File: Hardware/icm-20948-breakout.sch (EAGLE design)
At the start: 11 parts, among them J1 455-1750-1-ND, J2 455-1750-1-ND, U1 NCP563, U2 NTS0104, U3 ICM-20948

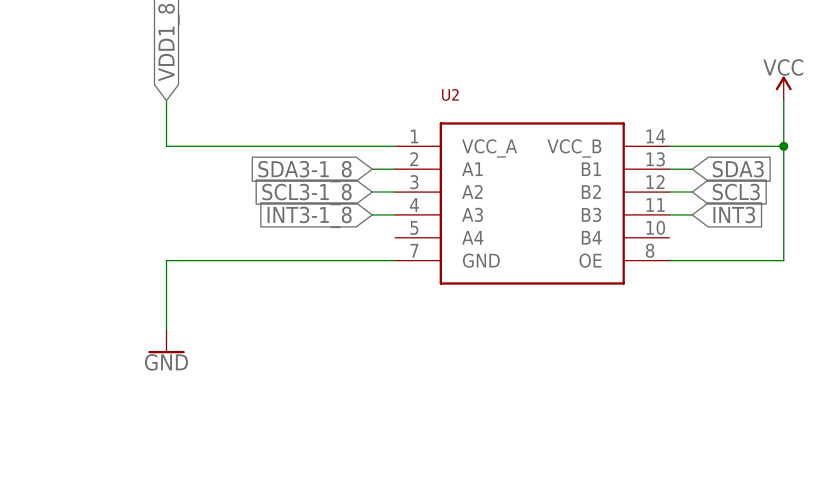
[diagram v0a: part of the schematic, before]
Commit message: Connected unused io pins on the level translator to ground.
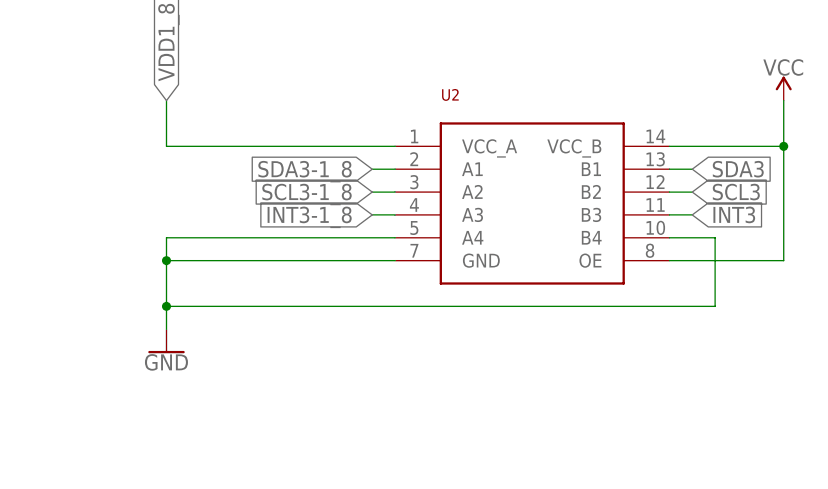
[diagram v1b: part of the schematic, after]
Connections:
- net GND: now also U2.A4, U2.B4
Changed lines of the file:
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@@
 <pinref part="GND4" gate="1" pin="GND"/>
 <pinref part="U2" gate="G$1" pin="GND"/>
-<wire x1="66.04" y1="20.32" x2="66.04" y2="12.7" width="0.1524" layer="91"/>
+<wire x1="66.04" y1="20.32" x2="66.04" y2="15.24" width="0.1524" layer="91"/>
+<wire x1="66.04" y1="15.24" x2="66.04" y2="12.7" width="0.1524" layer="91"/>
 <wire x1="91.44" y1="20.32" x2="66.04" y2="20.32" width="0.1524" layer="91"/>
+<pinref part="U2" gate="G$1" pin="A4"/>
+<wire x1="91.44" y1="22.86" x2="66.04" y2="22.86" width="0.1524" layer="91"/>
+<wire x1="66.04" y1="22.86" x2="66.04" y2="20.32" width="0.1524" layer="91"/>
+<junction x="66.04" y="20.32"/>
+<pinref part="U2" gate="G$1" pin="B4"/>
+<wire x1="121.92" y1="22.86" x2="127" y2="22.86" width="0.1524" layer="91"/>
+<wire x1="127" y1="22.86" x2="127" y2="15.24" width="0.1524" layer="91"/>
+<wire x1="127" y1="15.24" x2="66.04" y2="15.24" width="0.1524" layer="91"/>
+<junction x="66.04" y="15.24"/>
 </segment>
 <segment>

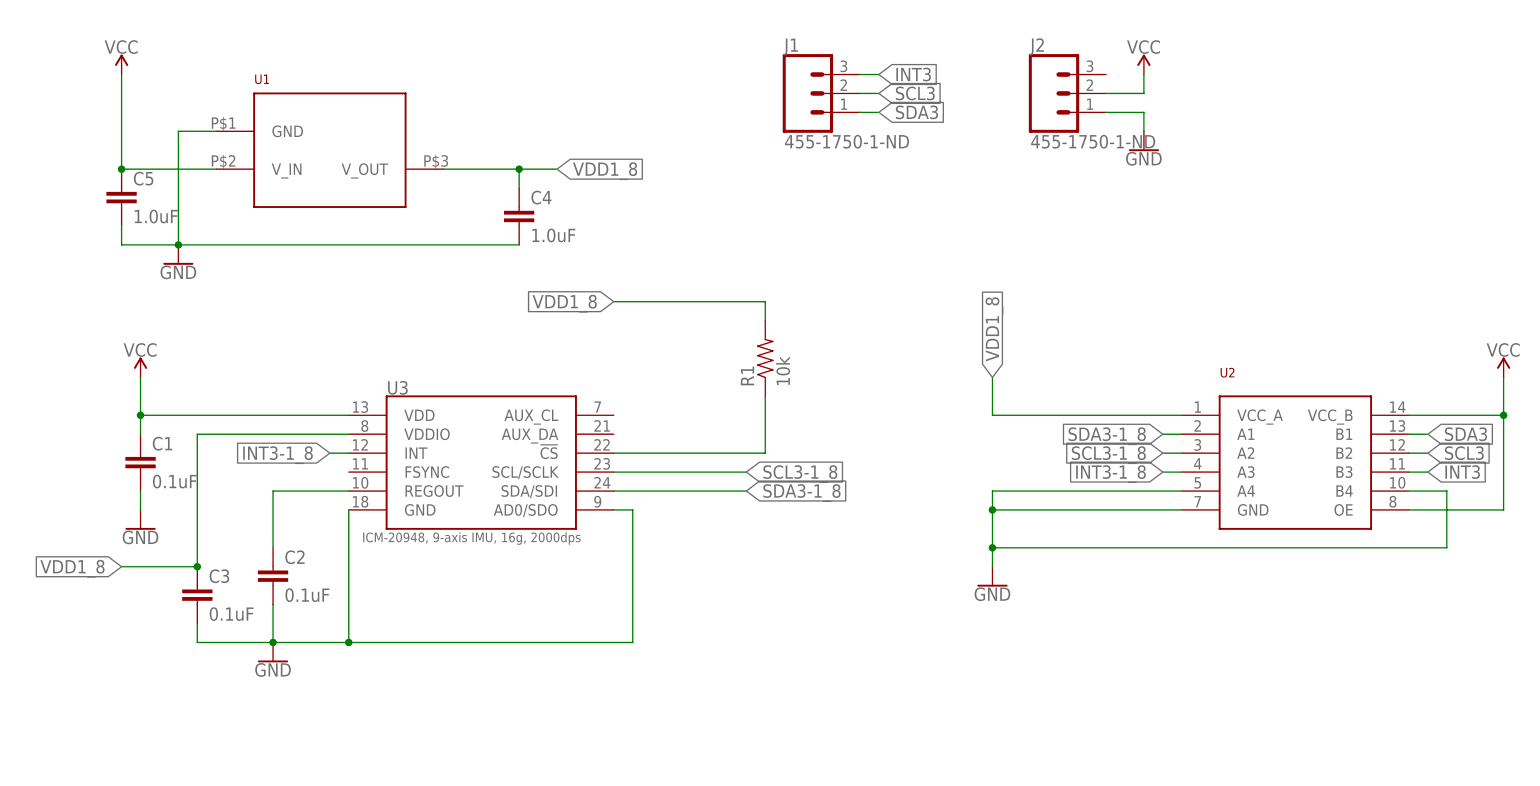
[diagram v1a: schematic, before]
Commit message: Redesign after comments. Changed footprints of capacitors. Removed routing under ICS. Connected nCS to level switcher to avoid a resistor. Added solder jumper to set address. Added ground planes on both sides.
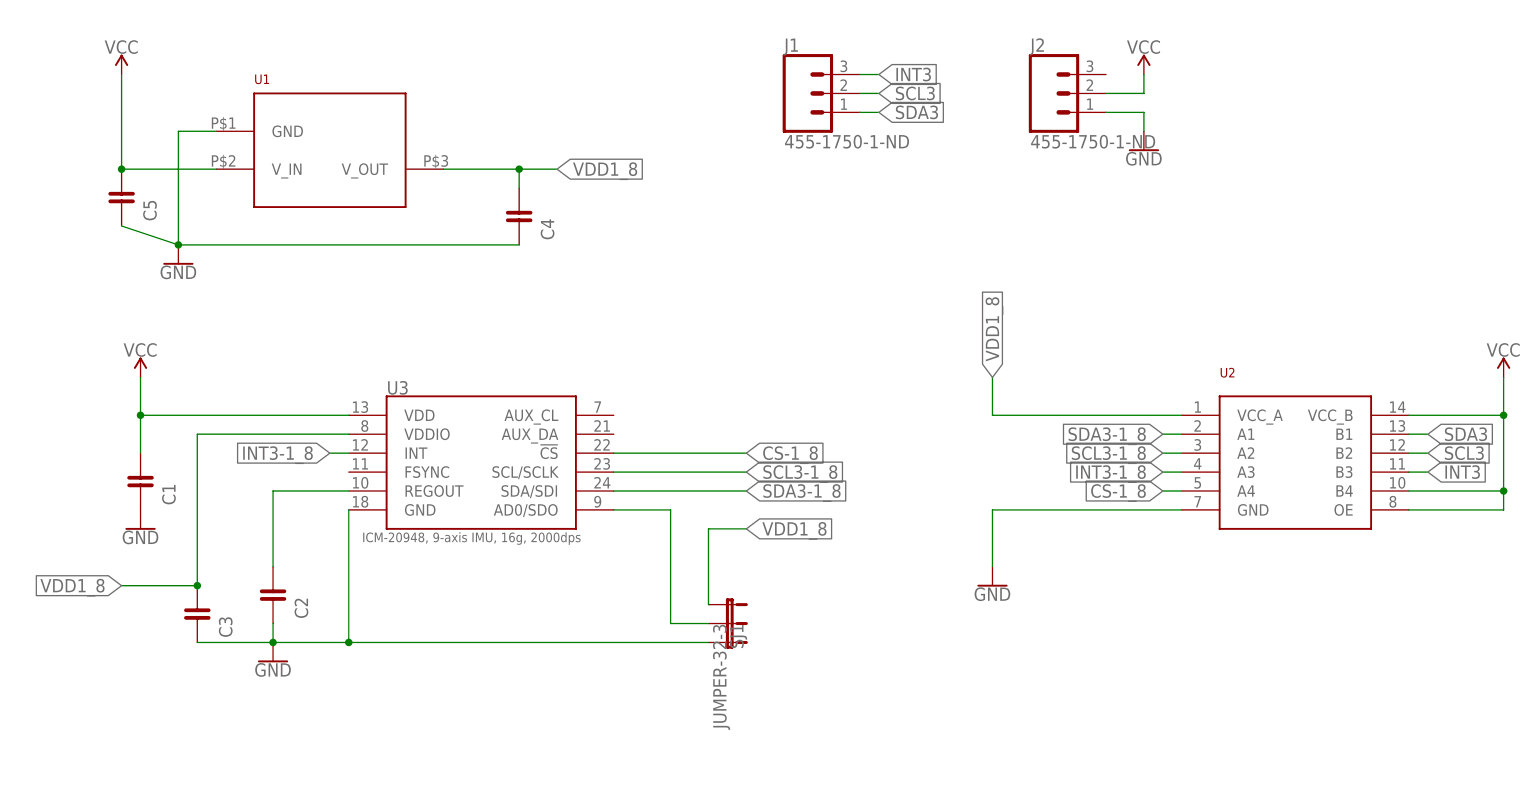
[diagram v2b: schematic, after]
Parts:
- removed R1: 10k, SparkFun-Passives:RESISTOR0402-RES
- added SJ1: JUMPER-32-3, SparkFun-Passives:JUMPER-32-3
- C1, C2, C3: device SparkFun-Capacitors:0.1UF-0402-16V-10% -> FaBo-Capacitor:CAPACITOR-0402
- C4, C5: device SparkFun-Capacitors:1.0UF-0402-16V-10% -> FaBo-Capacitor:CAPACITOR-0402
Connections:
- removed net N$4: R1.1, U3.!CS
- new net CS-1_8: U2.A4, U3.!CS
- new net N$2: SJ1.2, U3.AD0/SDO
- net GND: now also SJ1.3; no longer U2.A4, U2.B4, U3.AD0/SDO
- net VCC: now also U2.B4
- net VDD1_8: now also SJ1.1; no longer R1.2
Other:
- moved on the sheet: C1, C2, C3, C4, C5

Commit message: Updated ICM footprint. The design rules of OSH Park are now met.
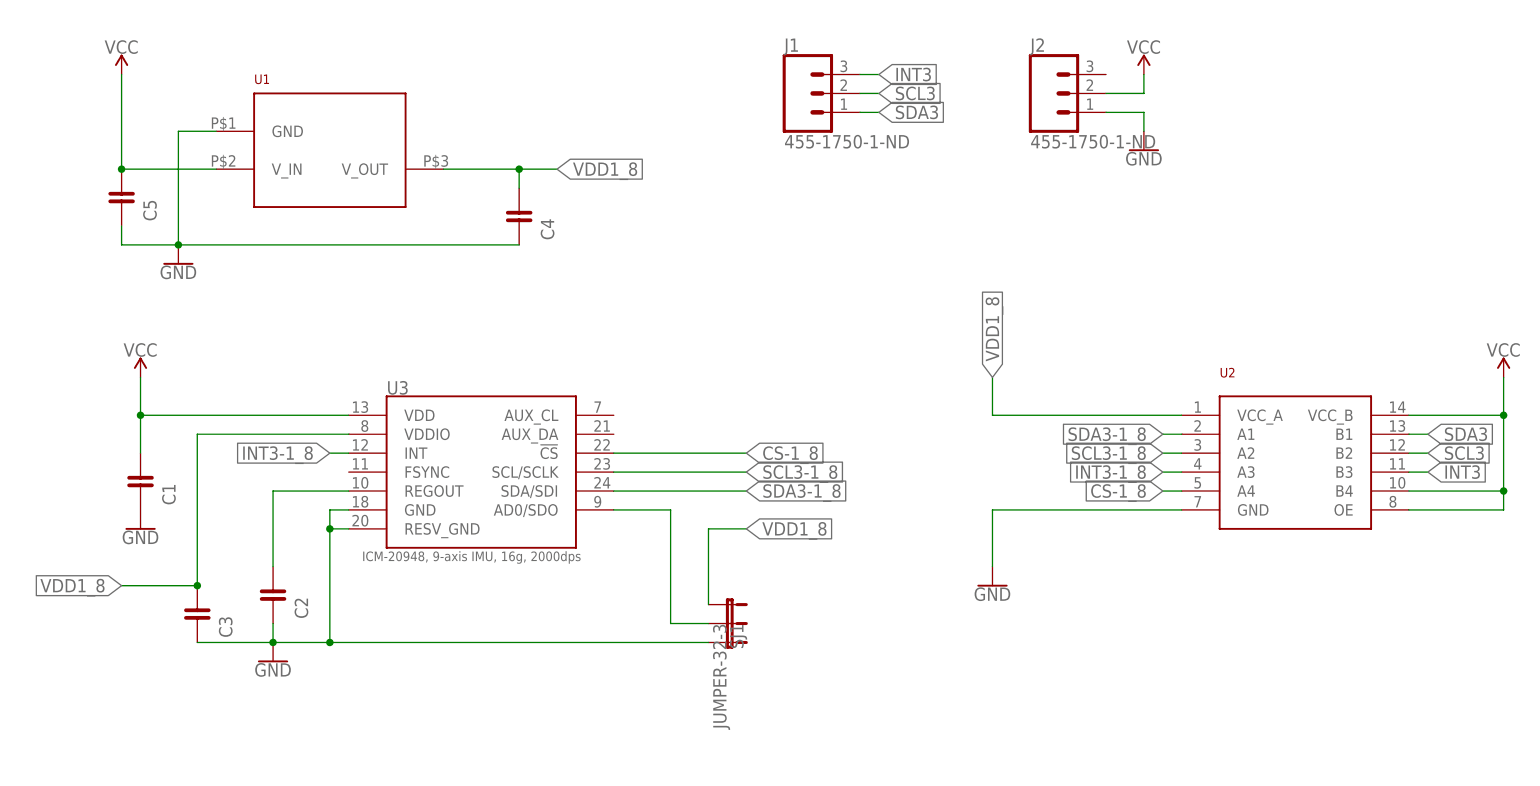
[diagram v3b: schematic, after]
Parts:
- U3: value ICM-20948 -> ICM-20948QFN24-COARSE; device david-mems:ICM-20948 -> david-mems:ICM-20948QFN24-COARSE
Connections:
- net GND: now also U3.RESV_GND
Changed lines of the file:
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@@
 </classes>
 <parts>
-<part name="U3" library="david-mems" deviceset="ICM-20948" device=""/>
+<part name="U3" library="david-mems" deviceset="ICM-20948" device="QFN24-COARSE" value="ICM-20948QFN24-COARSE"/>
 <part name="U2" library="david-mems" deviceset="NTS0104" device="DHVQFN14" value="NTS0104"/>
 <part name="C1" library="FaBo-Capacitor" deviceset="CAPACITOR" device="-0402" value="0.1uF"/>
@@
 <segment>
 <pinref part="GND2" gate="1" pin="GND"/>
-<pinref part="C5" gate="G$1" pin="2"/>
-<wire x1="-50.8" y1="58.42" x2="-43.18" y2="55.88" width="0.1524" layer="91"/>
 <junction x="-43.18" y="55.88"/>
 <pinref part="C4" gate="G$1" pin="2"/>
@@
 <wire x1="-38.1" y1="71.12" x2="-43.18" y2="71.12" width="0.1524" layer="91"/>
 <wire x1="-43.18" y1="71.12" x2="-43.18" y2="55.88" width="0.1524" layer="91"/>
+<wire x1="-43.18" y1="55.88" x2="-50.8" y2="55.88" width="0.1524" layer="91"/>
+<pinref part="C5" gate="G$1" pin="2"/>
+<wire x1="-50.8" y1="55.88" x2="-50.8" y2="58.42" width="0.1524" layer="91"/>
 </segment>
 <segment>
@@
 <pinref part="GND3" gate="1" pin="GND"/>
 <wire x1="-30.48" y1="5.08" x2="-30.48" y2="2.54" width="0.1524" layer="91"/>
-<pinref part="U3" gate="G$1" pin="GND"/>
-<wire x1="-20.32" y1="20.32" x2="-20.32" y2="2.54" width="0.1524" layer="91"/>
-<wire x1="-20.32" y1="2.54" x2="-30.48" y2="2.54" width="0.1524" layer="91"/>
 <junction x="-30.48" y="2.54"/>
-<wire x1="27.94" y1="2.54" x2="-20.32" y2="2.54" width="0.1524" layer="91"/>
-<junction x="-20.32" y="2.54"/>
+<wire x1="27.94" y1="2.54" x2="-22.86" y2="2.54" width="0.1524" layer="91"/>
 <pinref part="C3" gate="G$1" pin="2"/>
+<wire x1="-22.86" y1="2.54" x2="-30.48" y2="2.54" width="0.1524" layer="91"/>
 <wire x1="-40.64" y1="2.54" x2="-30.48" y2="2.54" width="0.1524" layer="91"/>
 <pinref part="SJ1" gate="G$1" pin="3"/>
+<pinref part="U3" gate="G$1" pin="GND"/>
+<wire x1="-20.32" y1="20.32" x2="-22.86" y2="20.32" width="0.1524" layer="91"/>
+<wire x1="-22.86" y1="20.32" x2="-22.86" y2="17.78" width="0.1524" layer="91"/>
+<junction x="-22.86" y="2.54"/>
+<pinref part="U3" gate="G$1" pin="RESV_GND"/>
+<wire x1="-22.86" y1="17.78" x2="-22.86" y2="2.54" width="0.1524" layer="91"/>
+<wire x1="-20.32" y1="17.78" x2="-22.86" y2="17.78" width="0.1524" layer="91"/>
+<junction x="-22.86" y="17.78"/>
 </segment>
 <segment>

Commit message: Fixed text layouts.
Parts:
- U3: value ICM-20948QFN24-COARSE -> ICM-20948
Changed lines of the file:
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@@
 </classes>
 <parts>
-<part name="U3" library="david-mems" deviceset="ICM-20948" device="QFN24-COARSE" value="ICM-20948QFN24-COARSE"/>
+<part name="U3" library="david-mems" deviceset="ICM-20948" device="QFN24-COARSE" value="ICM-20948"/>
 <part name="U2" library="david-mems" deviceset="NTS0104" device="DHVQFN14" value="NTS0104"/>
 <part name="C1" library="FaBo-Capacitor" deviceset="CAPACITOR" device="-0402" value="0.1uF"/>
